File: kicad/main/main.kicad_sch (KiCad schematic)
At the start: 55 parts, among them J1 Conn_01x02, J10 Conn_01x02, J2 Conn_01x03, J3 Conn_01x03, J4 Conn_01x02, J5 Conn_01x02, J6 Connector, USB-TYPE-C-16P, J7 Conn_01x02, J8 Conn_01x02, U2 XC6206P332MR, U5 RP2040, X1 X322512MSB4SI

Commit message: PCB Progress and Added LED_PWM signal
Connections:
- net LED_PWM: now also U5.9 (GPIO7)
- no-connect marks 20 -> 19
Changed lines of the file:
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@@
-	)
-	(no_connect
-		(at 121.92 88.9)
 	)
 	(no_connect
@@
 			)
 		)
+	)
+	(global_label "LED_PWM"
+		(shape input)
+		(at 121.92 88.9 0)
+		(fields_autoplaced yes)
+		(effects
+			(font
+				(size 1.27 1.27)
+			)
+			(justify left)
+		)
+		(property "Intersheetrefs" "${INTERSHEET_REFS}"
+			(at 133.4927 88.9 0)
+			(hide yes)
+			(show_name no)
+			(do_not_autoplace no)
+			(effects
+				(font
+					(size 1.27 1.27)
+				)
+				(justify left)
+			)
+		)

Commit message: adjusted power led resistor to decrease brightness, and added code to test onboard red led
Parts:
- removed R8: 430Ω, PCM_JLCPCB:R_0603, symbol PCM_JLCPCB-Resistors:0603,430Ω
- added R12: 2.2kΩ, PCM_JLCPCB:R_0402, symbol PCM_JLCPCB-Resistors:0402,2.2kΩ
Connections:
- net +5V: now also R12.1
- net at D3.2: now also R12.2

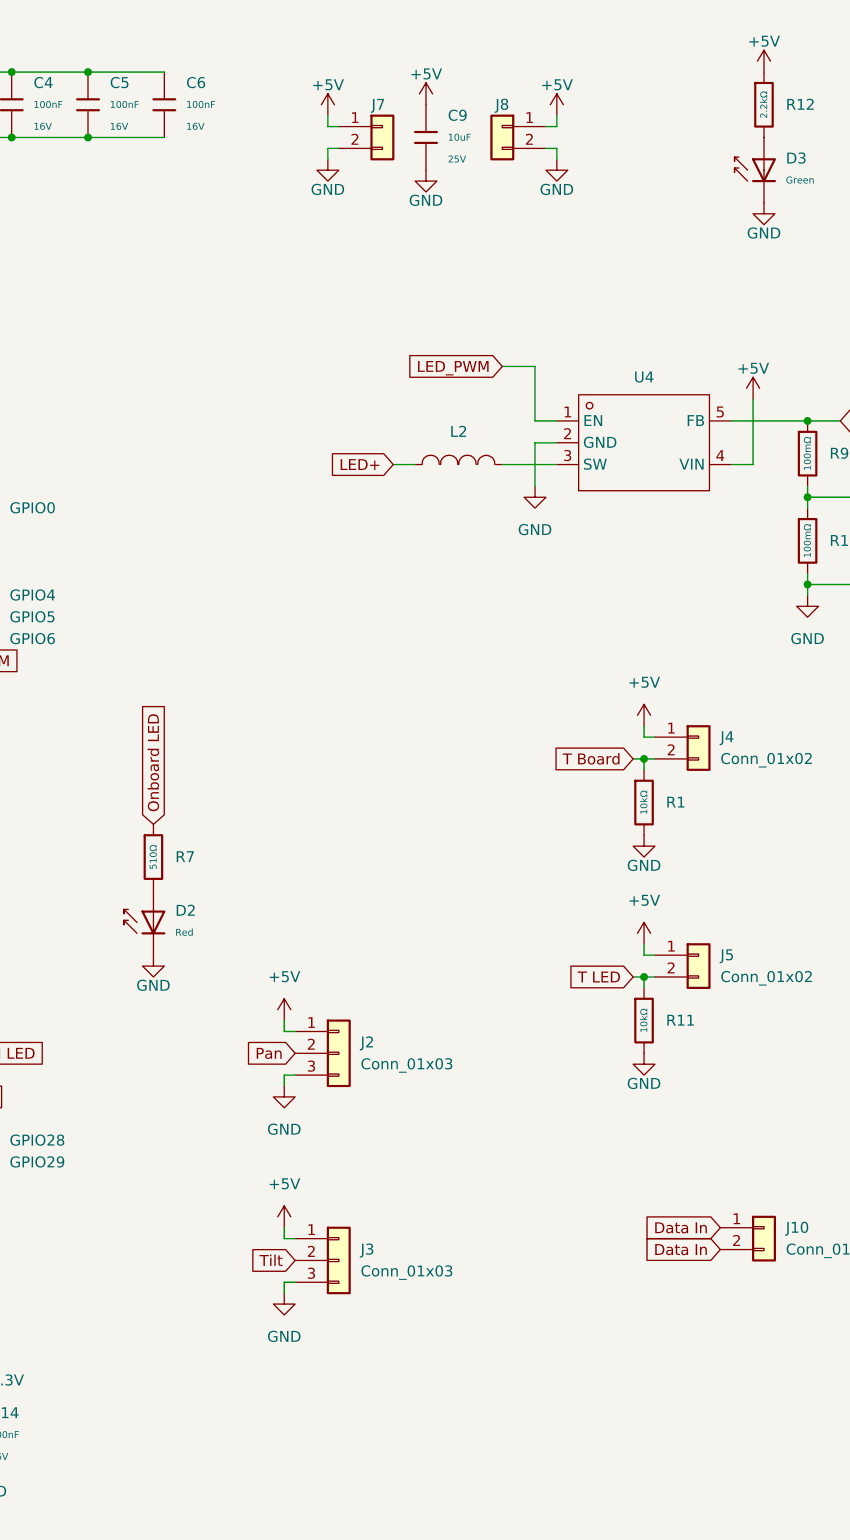
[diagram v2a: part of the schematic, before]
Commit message: Progress on fixing issues
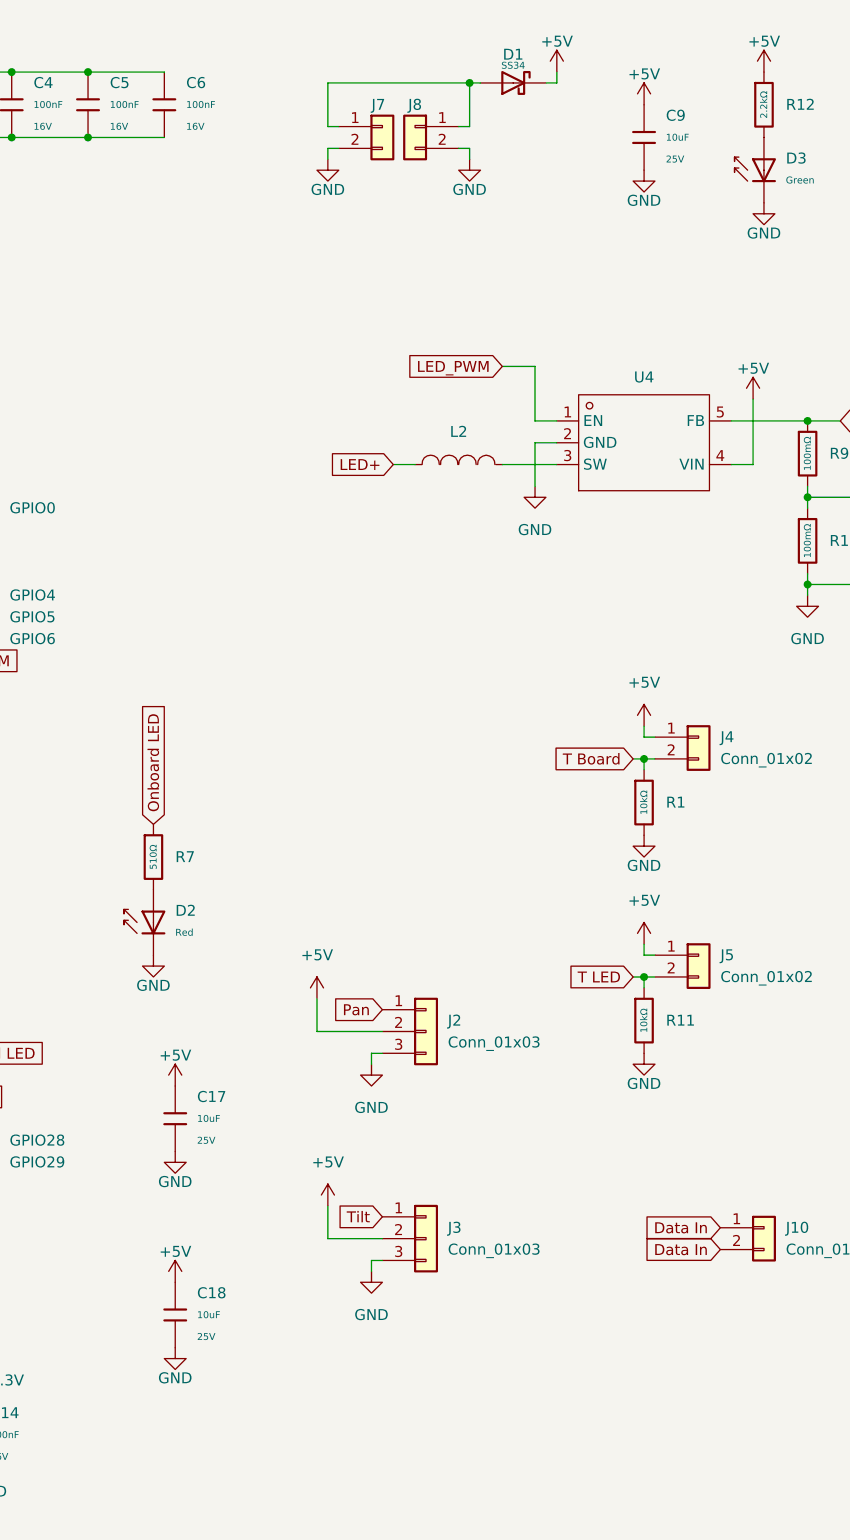
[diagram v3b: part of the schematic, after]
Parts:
- added C17, C18: 10uF, PCM_JLCPCB:C_0805, symbol PCM_JLCPCB-Capacitors:0805,10uF
- added D1: SS34, PCM_JLCPCB:D_SMA, symbol PCM_JLCPCB-Diodes:Schottky,SS34
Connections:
- net +5V: now also J2.2 (Pin_2), J3.2 (Pin_2), C17.1, C18.1, D1.1; no longer J2.1 (Pin_1), J3.1 (Pin_1), J7.1 (Pin_1), J8.1 (Pin_1)
- net GND: now also C17.2, C18.2
- net Pan: now also J2.1 (Pin_1); no longer J2.2 (Pin_2)
- net Tilt: now also J3.1 (Pin_1); no longer J3.2 (Pin_2)
- new net: D1.2, J7.1 (Pin_1), J8.1 (Pin_1)
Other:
- moved on the sheet: C9, J2, J3, J8
